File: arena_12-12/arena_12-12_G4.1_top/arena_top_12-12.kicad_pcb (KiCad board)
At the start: 2 copper layers, 228.6 x 228.6 mm, 41 parts, among them J4 Barrel_Jack, P1 CONN15, P10 CONN15, P11 CONN15, P12 CONN15, P2 CONN15, P3 CONN15, P4 CONN15, P5 CONN15, P6 CONN15, P7 CONN15, P8 CONN15, P9 CONN15

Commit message: bump version
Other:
- board text added: "${ISSUE_DATE}"
- board text added: "${TITLE} ${REVISION}"
- board text removed: "12-12 Teensy G4.1 Arena Top v0.3.3"
- board text removed: "2024-12-23"

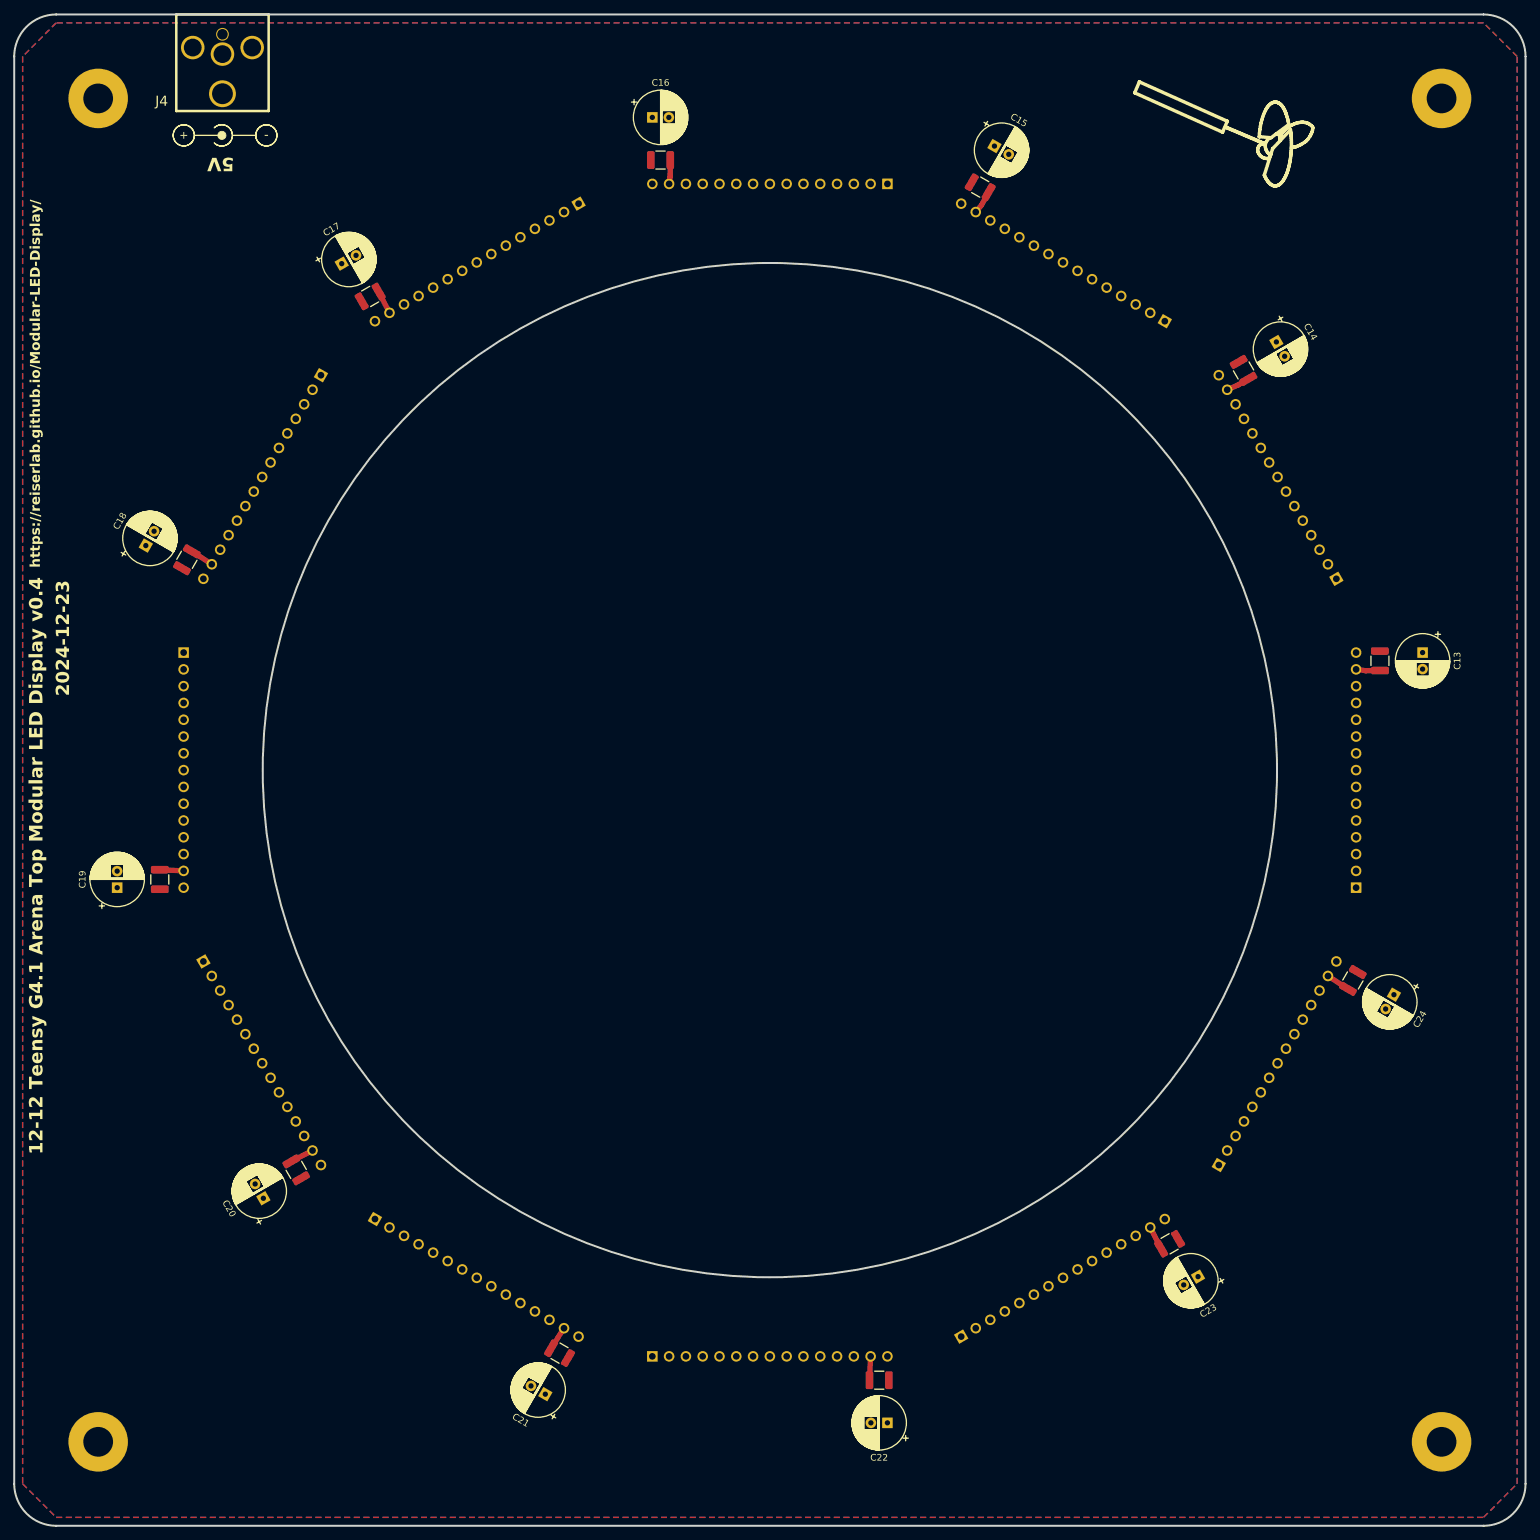
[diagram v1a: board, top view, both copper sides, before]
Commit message: One-sided version
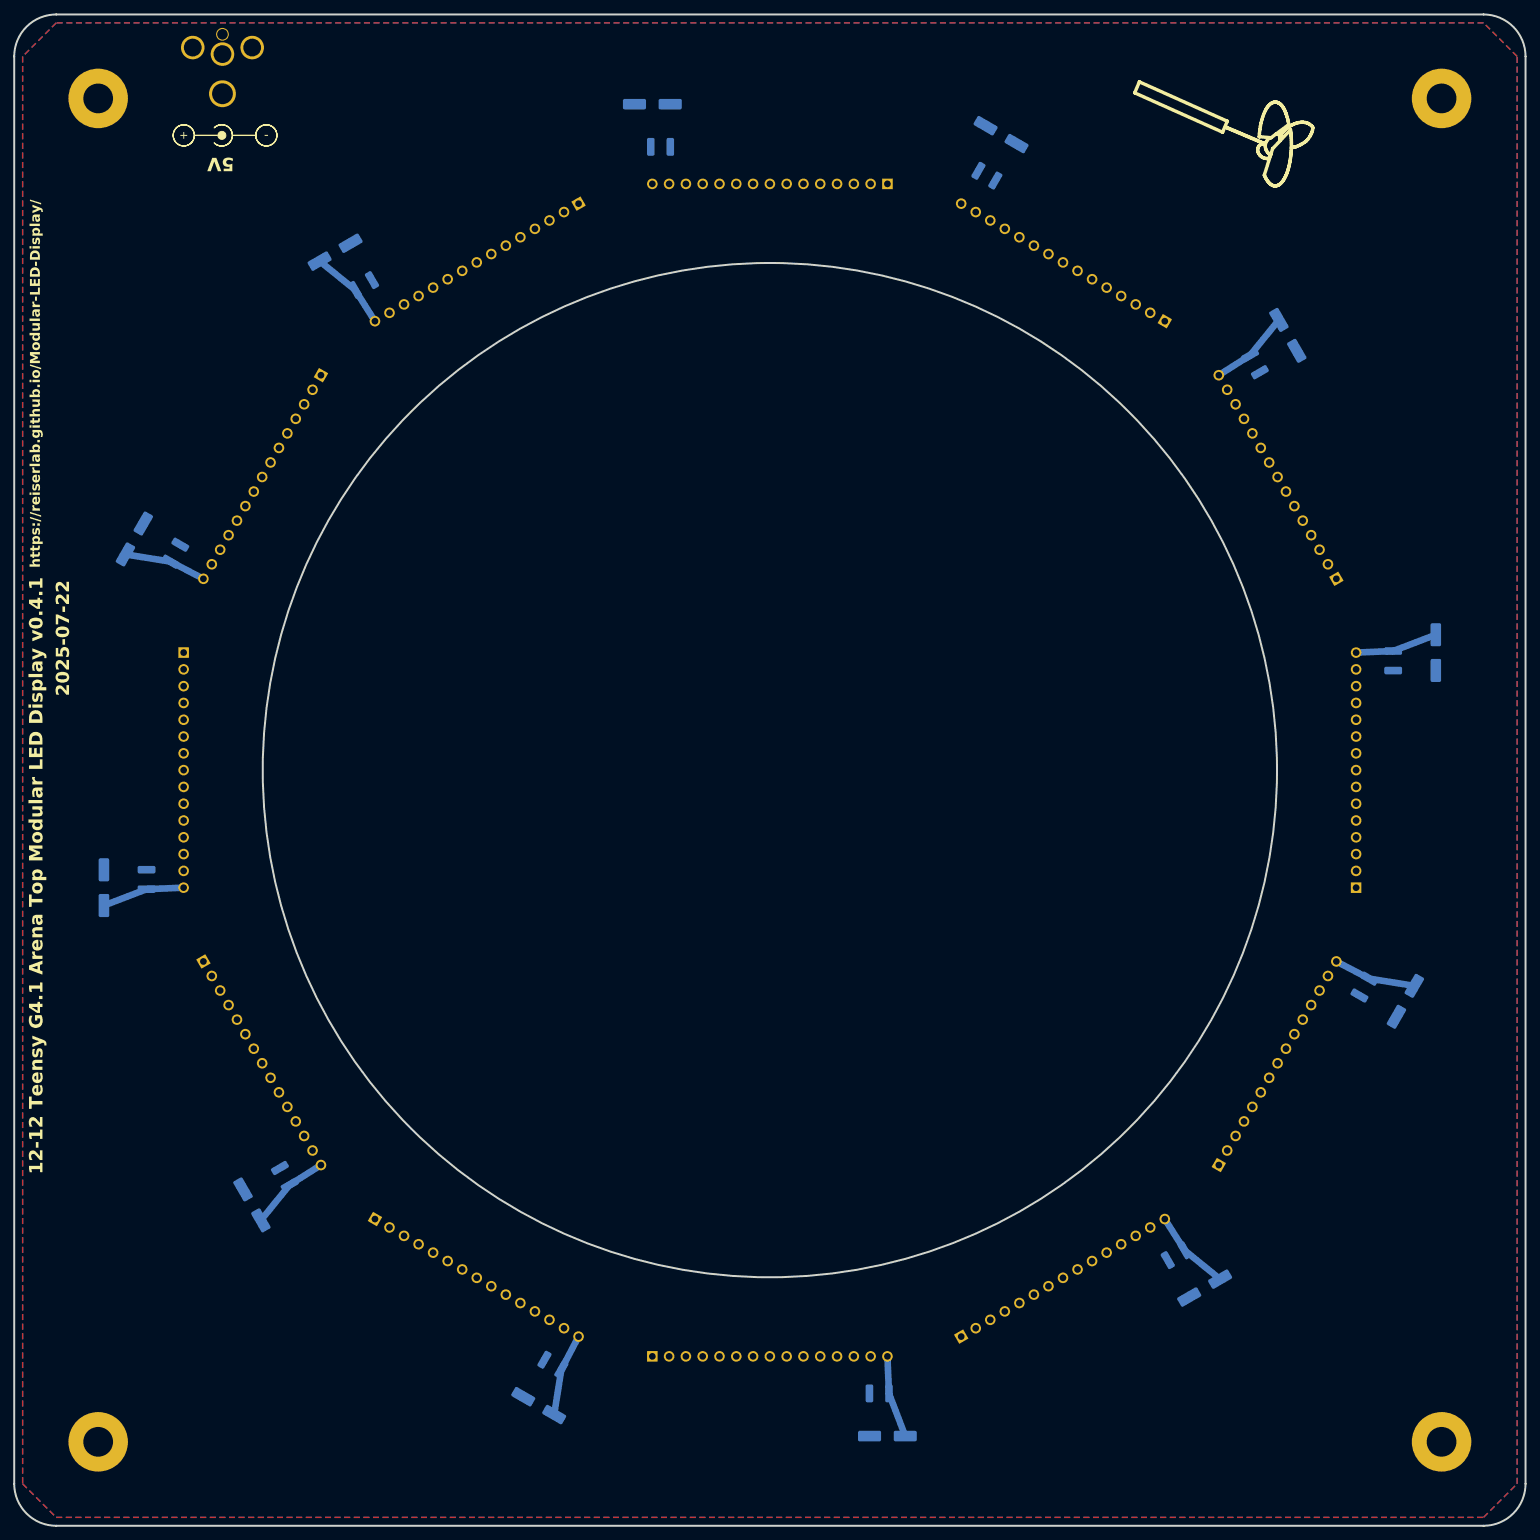
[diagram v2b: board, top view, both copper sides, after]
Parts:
- C1, C10, C11, C12, C2, C3, C4, C5, C6, C7, C8, C9, J4: moved to B.Cu
- C13, C14, C15, C16, C17, C18, C19, C20, C21, C22, C23, C24: footprint Capacitor_THT:CP_Radial_D8.0mm_P2.50mm -> Capacitor_SMD:CP_Elec_6.3x7.7; moved to B.Cu
- moved C11 2.00 mm to (239.3, 251.2)
- moved C12 2.00 mm to (267.7, 210.6)
- moved C2 2.00 mm to (251.2, 116.3)
- moved C21 2.00 mm to (142.8, 273.9)
- moved C24 2.00 mm to (273.9, 212.8)
- moved C9 2.00 mm to (145.0, 267.7)
- moved C15 2.00 mm to (212.8, 81.7)
- moved C17 2.00 mm to (112.0, 99.5)
- moved C18 2.00 mm to (81.7, 142.8)
- moved C20 2.00 mm to (99.5, 243.6)
- moved C3 2.00 mm to (210.6, 87.9)
- moved C5 2.00 mm to (116.3, 104.4)
- moved C6 2.00 mm to (87.9, 145.0)
- moved C8 2.00 mm to (104.4, 239.3)
- moved C14 2.00 mm to (256.1, 112.0)
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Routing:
- net +5V: track 0.00 -> 125.3 mm
- net GND: track 43.3 -> 0.00 mm

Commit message: cleanup top, v0.4.2
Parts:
- J4: footprint arena_custom:DCJACK_2PIN_HIGHCURRENT -> Connector_BarrelJack:BarrelJack_CUI_PJ-036AH-SMT_Horizontal
- moved J4 11.9 mm to (95.4, 75.4), turned to 0 degrees
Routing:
- net +5V: track 125.3 -> 129.1 mm, vias 0 -> 1
